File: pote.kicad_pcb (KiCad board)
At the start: 2 copper layers, 8 parts, among them J1 Conn_01x01, J2 Conn_01x01, J3 Conn_01x01, J4 Conn_01x01, J5 Conn_01x01, U1 Opamp_Quad_Generic, U2 Opamp_Quad_Generic

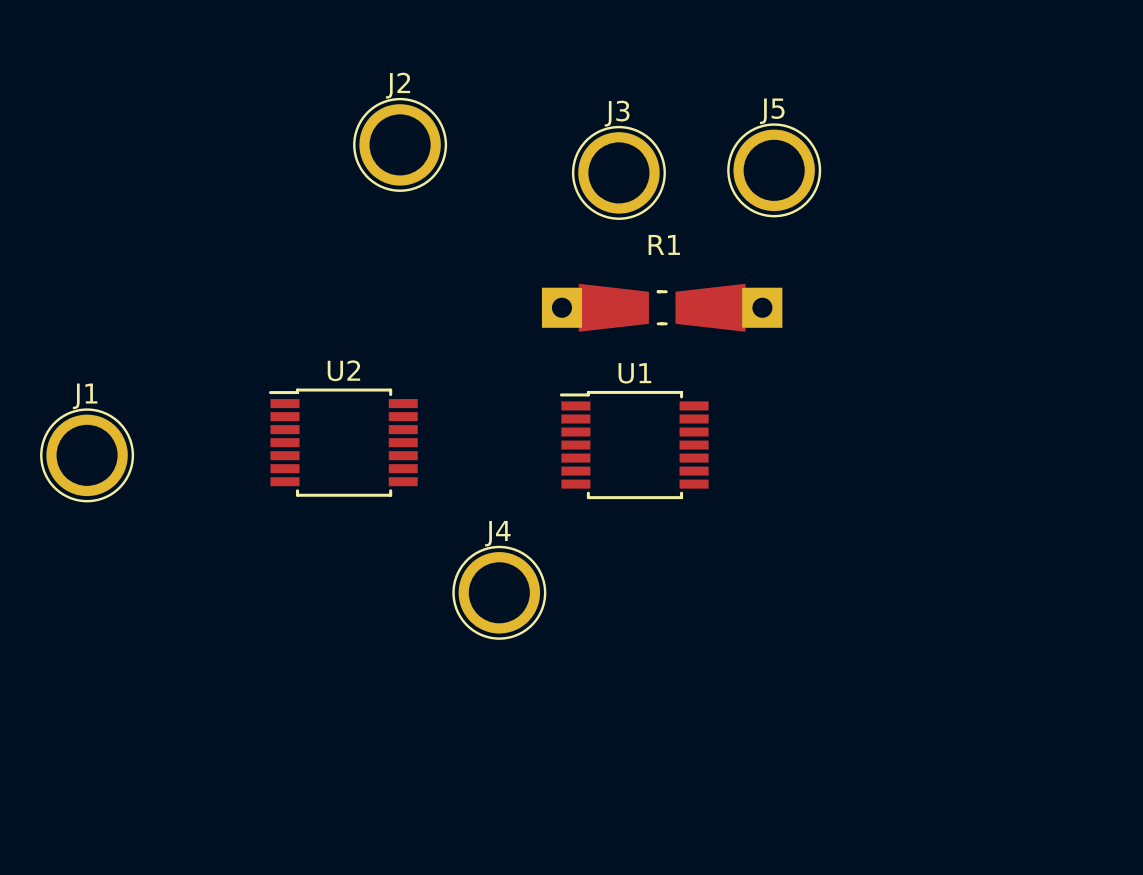
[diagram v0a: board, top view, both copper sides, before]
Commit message: placement 1st cut and routing WIP
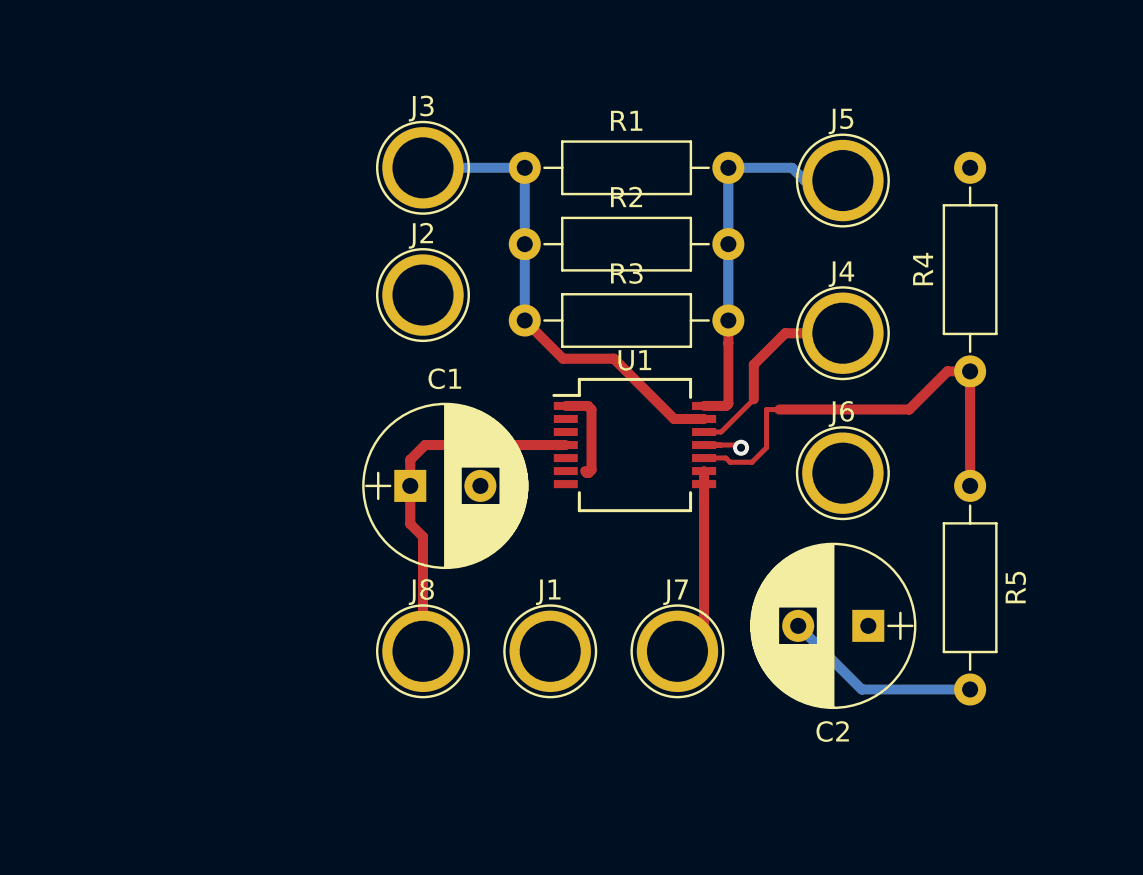
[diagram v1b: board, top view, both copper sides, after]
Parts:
- removed U2: Opamp_Quad_Generic, Housings_SSOP:TSSOP-14_4.4x5mm_Pitch0.65mm
- added C1: 100u, Capacitors_THT:CP_Radial_D8.0mm_P3.50mm, F.Cu at (160.0, 90.8)
- added C2: 100u, Capacitors_THT:CP_Radial_D8.0mm_P3.50mm, F.Cu at (182.9, 97.8)
- added J6: Conn_01x01, Connectors:1pin, F.Cu at (181.6, 90.2)
- added J7: Conn_01x01, Connectors:1pin, F.Cu at (173.4, 99.1)
- added J8: Conn_01x01, Connectors:1pin, F.Cu at (160.7, 99.1)
- added R2: 100k, Resistors_THT:R_Axial_DIN0207_L6.3mm_D2.5mm_P10.16mm_Horizontal, F.Cu at (165.7, 78.7)
- added R3: 100k, Resistors_THT:R_Axial_DIN0207_L6.3mm_D2.5mm_P10.16mm_Horizontal, F.Cu at (165.7, 82.5)
- added R4: 100k, Resistors_THT:R_Axial_DIN0207_L6.3mm_D2.5mm_P10.16mm_Horizontal, F.Cu at (188.0, 85.1)
- added R5: 100k, Resistors_THT:R_Axial_DIN0207_L6.3mm_D2.5mm_P10.16mm_Horizontal, F.Cu at (188.0, 90.8)
- R1: value 1k -> 100k; footprint Resistors_Universal:Resistor_SMD+THTuniversal_0805to1206_RM10_HandSoldering -> Resistors_THT:R_Axial_DIN0207_L6.3mm_D2.5mm_P10.16mm_Horizontal
- U1: footprint Housings_SSOP:TSSOP-14_4.4x5mm_Pitch0.65mm -> Housings_SSOP:SSOP-14_5.3x6.2mm_Pitch0.65mm
- moved J1 25.1 mm to (167.0, 99.1)
- moved J4 21.5 mm to (181.6, 83.2)
- moved R1 9.79 mm to (165.7, 74.9)
- moved J3 9.78 mm to (160.7, 74.9)
- moved J2 7.58 mm to (160.7, 81.3)
- moved J5 3.47 mm to (181.6, 75.6)
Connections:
- U1 pad 1: Net-(J5-Pad1) -> Net-(U1-Pad1)
- U1 pad 10: (no net) -> Net-(C2-Pad1)
- U1 pad 11: (no net) -> GNDA
- U1 pad 12: (no net) -> Net-(J4-Pad1)
- U1 pad 13: (no net) -> Net-(J3-Pad1)
- U1 pad 14: (no net) -> Net-(J5-Pad1)
- U1 pad 2: Net-(J3-Pad1) -> Net-(U1-Pad1)
- U1 pad 3: Net-(J4-Pad1) -> Net-(J2-Pad1)
- U1 pad 4: (no net) -> VCC
- U1 pad 5: (no net) -> Net-(J1-Pad1)
- U1 pad 6: (no net) -> Net-(U1-Pad1)
- U1 pad 7: (no net) -> Net-(J2-Pad1)
- U1 pad 8: (no net) -> Net-(J7-Pad1)
- U1 pad 9: (no net) -> Net-(J7-Pad1)
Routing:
- net Net-(J3-Pad1): track 0.00 -> 23.7 mm
- net Net-(C2-Pad1): track 0.00 -> 22.1 mm
- net Net-(J5-Pad1): track 0.00 -> 19.0 mm
- net VCC: track 0.00 -> 17.9 mm
- net GNDA: track 0.00 -> 12.6 mm, vias 0 -> 1
- net Net-(J4-Pad1): track 0.00 -> 9.98 mm
- net Net-(J7-Pad1): track 0.00 -> 9.55 mm
- net Net-(U1-Pad1): track 0.00 -> 4.79 mm

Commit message: routing 1st cut
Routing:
- net VCC: track 17.9 -> 64.1 mm
- net Net-(J2-Pad1): track 0.00 -> 31.5 mm, vias 0 -> 1
- net Net-(C2-Pad1): track 22.1 -> 34.6 mm
- net Net-(J1-Pad1): track 0.00 -> 11.0 mm
- net Net-(U1-Pad1): track 4.79 -> 6.62 mm
- added copper zone on B.Cu, net GNDA
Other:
- board outline added: 39.4 x 36.8 mm
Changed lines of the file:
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@@
-(kicad_pcb (version 20171130) (host pcbnew 5.1.5-52549c5~84~ubuntu16.04.1)
+(kicad_pcb (version 20171130) (host pcbnew 5.1.4-e60b266~84~ubuntu18.04.1)
   (general
     (thickness 1.6)
-    (drawings 0)
-    (tracks 52)
+    (drawings 4)
+    (tracks 84)
     (zones 0)
     (modules 16)
@@
       (net 6 VCC))
   )
+  (gr_line (start 153.67 105.41) (end 153.67 68.58) (layer Edge.Cuts) (width 0.05))
+  (gr_line (start 193.04 105.41) (end 153.67 105.41) (layer Edge.Cuts) (width 0.05))
+  (gr_line (start 193.04 68.58) (end 193.04 105.41) (layer Edge.Cuts) (width 0.05))
+  (gr_line (start 153.67 68.58) (end 193.04 68.58) (layer Edge.Cuts) (width 0.05))
+  (segment (start 166.934001 89.415001) (end 166.37 89.979002) (width 0.25) (layer F.Cu) (net 1))
+  (segment (start 167.784001 89.415001) (end 166.934001 89.415001) (width 0.25) (layer F.Cu) (net 1))
+  (segment (start 166.37 98.425) (end 167.005 99.06) (width 0.5) (layer F.Cu) (net 1))
+  (segment (start 166.37 89.979002) (end 166.37 98.425) (width 0.5) (layer F.Cu) (net 1))
+  (segment (start 167.784001 88.115001) (end 165.585001 88.115001) (width 0.25) (layer F.Cu) (net 2))
+  (segment (start 165.585001 88.115001) (end 163.83 86.36) (width 0.25) (layer F.Cu) (net 2))
+  (segment (start 160.655 83.185) (end 160.655 81.28) (width 0.5) (layer F.Cu) (net 2))
+  (segment (start 163.83 86.36) (end 160.655 83.185) (width 0.5) (layer F.Cu) (net 2))
+  (via (at 171.45 90.17) (size 0.8) (drill 0.4) (layers F.Cu B.Cu) (net 2))
+  (segment (start 170.204999 91.415001) (end 171.45 90.17) (width 0.5) (layer F.Cu) (net 2))
+  (segment (start 168.884001 91.415001) (end 170.204999 91.415001) (width 0.5) (layer F.Cu) (net 2))
+  (segment (start 167.784001 90.715001) (end 168.184001 90.715001) (width 0.5) (layer F.Cu) (net 2))
+  (segment (start 168.184001 90.715001) (end 168.884001 91.415001) (width 0.5) (layer F.Cu) (net 2))
+  (segment (start 171.45 90.17) (end 171.45 87.63) (width 0.5) (layer B.Cu) (net 2))
+  (segment (start 171.45 87.63) (end 170.18 87.63) (width 0.5) (layer B.Cu) (net 2))
+  (segment (start 170.18 87.63) (end 168.91 86.36) (width 0.5) (layer B.Cu) (net 2))
+  (segment (start 165.735 86.36) (end 160.655 81.28) (width 0.5) (layer B.Cu) (net 2))
+  (segment (start 168.91 86.36) (end 165.735 86.36) (width 0.5) (layer B.Cu) (net 2))
   (segment (start 160.655 74.93) (end 165.735 74.93) (width 0.5) (layer B.Cu) (net 3))
   (segment (start 165.735 74.93) (end 165.735 82.55) (width 0.5) (layer B.Cu) (net 3))
@@
   (segment (start 160.655 93.345) (end 160.655 99.06) (width 0.5) (layer F.Cu) (net 6))
   (segment (start 160.02 92.71) (end 160.655 93.345) (width 0.5) (layer F.Cu) (net 6))
+  (segment (start 187.96 74.93) (end 186.69 74.93) (width 0.5) (layer B.Cu) (net 6))
+  (segment (start 186.69 74.93) (end 185.42 76.2) (width 0.5) (layer B.Cu) (net 6))
+  (segment (start 185.42 76.2) (end 185.42 91.44) (width 0.5) (layer B.Cu) (net 6))
+  (segment (start 185.42 91.44) (end 182.88 93.98) (width 0.5) (layer B.Cu) (net 6))
+  (segment (start 165.735 93.98) (end 160.655 99.06) (width 0.5) (layer B.Cu) (net 6))
+  (segment (start 182.88 93.98) (end 165.735 93.98) (width 0.5) (layer B.Cu) (net 6))
   (segment (start 182.555 100.965) (end 179.38 97.79) (width 0.5) (layer B.Cu) (net 7))
   (segment (start 187.96 100.965) (end 182.555 100.965) (width 0.5) (layer B.Cu) (net 7))
@@
   (segment (start 187.96 85.09) (end 186.82863 85.09) (width 0.5) (layer F.Cu) (net 9))
   (segment (start 184.92363 86.995) (end 178.435 86.995) (width 0.5) (layer F.Cu) (net 9))
-  (segment (start 177.8 86.995) (end 178.435 86.995) (width 0.25) (layer F.Cu) (net 9))
+  (segment (start 177.8 86.995) (end 178.435 86.995) (width 0.5) (layer F.Cu) (net 9))
   (segment (start 174.684001 89.415001) (end 175.775001 89.415001) (width 0.25) (layer F.Cu) (net 9))
   (segment (start 175.985001 89.625001) (end 177.074999 89.625001) (width 0.25) (layer F.Cu) (net 9))
   (segment (start 175.775001 89.415001) (end 175.985001 89.625001) (width 0.25) (layer F.Cu) (net 9))
   (segment (start 177.074999 89.625001) (end 177.8 88.9) (width 0.25) (layer F.Cu) (net 9))
-  (segment (start 177.8 88.9) (end 177.8 86.995) (width 0.25) (layer F.Cu) (net 9))
+  (segment (start 177.8 88.9) (end 177.8 86.995) (width 0.5) (layer F.Cu) (net 9))
+  (segment (start 177.8 88.9) (end 179.07 90.17) (width 0.5) (layer F.Cu) (net 9))
+  (segment (start 179.07 90.17) (end 181.61 90.17) (width 0.5) (layer F.Cu) (net 9))
+  (segment (start 181.61 90.17) (end 181.61 91.44) (width 0.25) (layer F.Cu) (net 9))
+  (segment (start 182.88 92.71) (end 182.88 97.79) (width 0.5) (layer F.Cu) (net 9))
+  (segment (start 181.61 91.44) (end 182.88 92.71) (width 0.5) (layer F.Cu) (net 9))
   (segment (start 168.884001 86.815001) (end 169.064 86.995) (width 0.5) (layer F.Cu) (net 10))
   (segment (start 167.784001 86.815001) (end 168.884001 86.815001) (width 0.5) (layer F.Cu) (net 10))
@@
   (segment (start 168.925 90.155) (end 168.834002 90.155) (width 0.5) (layer F.Cu) (net 10))
   (segment (start 169.064 90.016) (end 168.925 90.155) (width 0.5) (layer F.Cu) (net 10))
+  (segment (start 167.784001 86.815001) (end 167.784001 87.465001) (width 0.5) (layer F.Cu) (net 10))
+  (segment (start 168.835001 90.065001) (end 168.925 90.155) (width 0.25) (layer F.Cu) (net 10))
+  (segment (start 167.784001 90.065001) (end 168.835001 90.065001) (width 0.25) (layer F.Cu) (net 10))
+  (zone (net 7) (net_name GNDA) (layer B.Cu) (hatch edge 0.508)
+    (connect_pads (clearance 0.508))
+    (min_thickness 0.254)
+    (fill yes (arc_segments 32) (thermal_gap 0.508) (thermal_bridge_width 0.508))
+    (polygon
+      (pts
+        (xy 154.94 69.85) (xy 191.77 69.85) (xy 191.77 104.14) (xy 154.94 104.14)
+      )
+    )
+  )
 )

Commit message: Modified by kou
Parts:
- removed J4, J5, J6, J7, J8: Conn_01x01, Connectors:1pin
- C1, C2, R1, R2, R3, R4, R5, U1: moved to B.Cu
- J1: value Conn_01x01 -> Conn_01x03; footprint Connectors:1pin -> Connector_PinHeader_2.54mm:PinHeader_1x03_P2.54mm_Vertical; moved to B.Cu
- J2: value Conn_01x01 -> Conn_01x03; footprint Connectors:1pin -> Connector_PinHeader_2.54mm:PinHeader_1x07_P2.54mm_Vertical; moved to B.Cu
- J3: value Conn_01x01 -> Conn_01x03; footprint Connectors:1pin -> Connector_PinHeader_2.54mm:PinHeader_1x05_P2.54mm_Vertical; moved to B.Cu
- moved J3 37.4 mm to (181.9, 105.8)
- moved R1 29.6 mm to (165.7, 104.5)
- moved R2 21.9 mm to (165.7, 100.7)
- moved R5 14.8 mm to (188.2, 105.6), turned to 90 degrees
- moved C2 14.6 mm to (181.2, 83.3), turned to 90 degrees
- moved J2 14.6 mm to (174.8, 77.8), turned to 90 degrees
- moved R3 14.3 mm to (165.7, 96.9)
- moved J1 9.43 mm to (159.2, 104.4)
- moved R4 4.94 mm to (188.2, 90.0)
- moved C1 3.66 mm to (162.8, 88.4), turned to 180 degrees
- moved U1 1.89 mm to (171.2, 90.7)
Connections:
- J3 pad 1: Net-(J3-Pad1) -> Net-(C2-Pad1)
- R1 pad 1: Net-(J3-Pad1) -> Net-(J1-Pad1)
- R1 pad 2: Net-(J5-Pad1) -> Net-(J3-Pad3)
- R2 pad 1: Net-(J3-Pad1) -> Net-(J1-Pad1)
- R2 pad 2: Net-(J5-Pad1) -> Net-(J3-Pad3)
- R3 pad 1: Net-(J3-Pad1) -> Net-(J1-Pad1)
- R3 pad 2: Net-(J5-Pad1) -> Net-(J3-Pad3)
- U1 pad 12: Net-(J4-Pad1) -> Net-(J3-Pad5)
- U1 pad 13: Net-(J3-Pad1) -> Net-(J1-Pad1)
- U1 pad 14: Net-(J5-Pad1) -> Net-(J3-Pad3)
- U1 pad 3: Net-(J2-Pad1) -> Net-(J1-Pad3)
- U1 pad 5: Net-(J1-Pad1) -> Net-(J2-Pad3)
- U1 pad 7: Net-(J2-Pad1) -> Net-(J1-Pad3)
- U1 pad 8: Net-(J7-Pad1) -> Net-(J2-Pad1)
- U1 pad 9: Net-(J7-Pad1) -> Net-(J2-Pad1)
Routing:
- net Net-(J1-Pad3): track 0.00 -> 40.9 mm
- net Net-(J3-Pad1): track 23.7 -> 0.00 mm
- net Net-(J5-Pad1): track 19.0 -> 0.00 mm
- net Net-(J3-Pad3): track 0.00 -> 18.8 mm
- net VCC: track 64.1 -> 46.1 mm
- net Net-(J2-Pad1): track 31.5 -> 14.6 mm, vias 1 -> 0
- net Net-(J1-Pad1): track 11.0 -> 26.8 mm
- net Net-(J2-Pad3): track 0.00 -> 15.7 mm
- net Net-(C2-Pad1): track 34.6 -> 47.5 mm
- net Net-(J4-Pad1): track 9.98 -> 0.00 mm
- net Net-(J7-Pad1): track 9.55 -> 0.00 mm
- net Net-(J3-Pad5): track 0.00 -> 8.99 mm
- net GNDA: track 12.6 -> 3.90 mm, vias 1 -> 0
